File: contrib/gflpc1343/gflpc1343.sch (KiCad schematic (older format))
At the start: 38 parts, among them J1 USB-MICRO-B, P1 GOODFET, P2 SWD, P3 ISP, P4 EXPANSION, Q1 PNP, U1 LPC1343FBD48, U2 AP7333, X1 XTAL4PIN

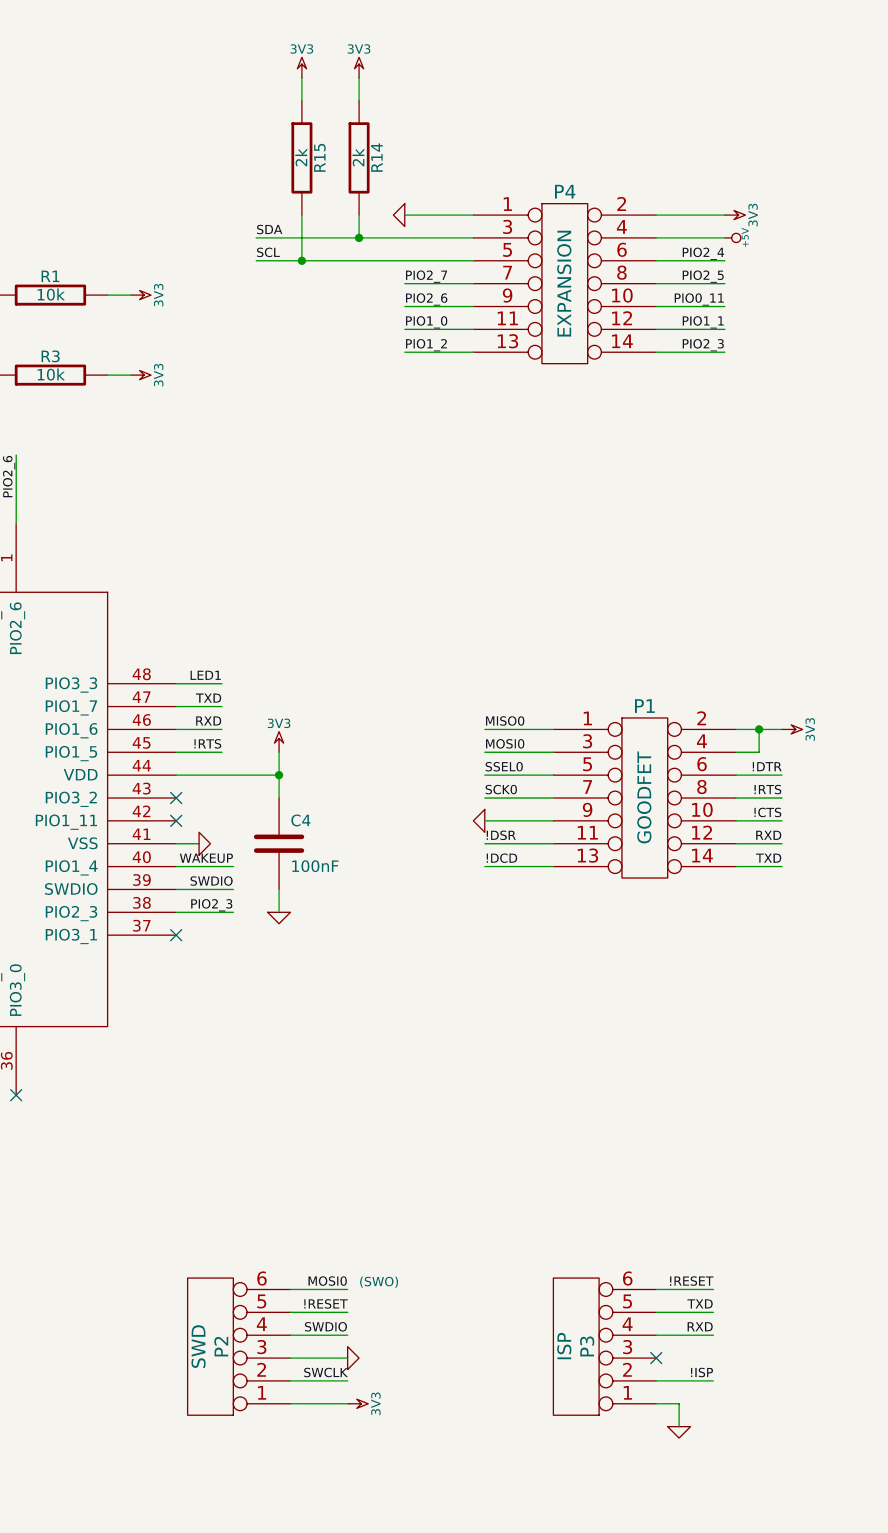
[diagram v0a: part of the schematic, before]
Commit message: gflpc1343 parts selection, paste clearance
git-svn-id: https://svn.code.sf.net/p/goodfet/code@1323 12e2690d-a6be-4b82-a7b7-67c4a43b65c8
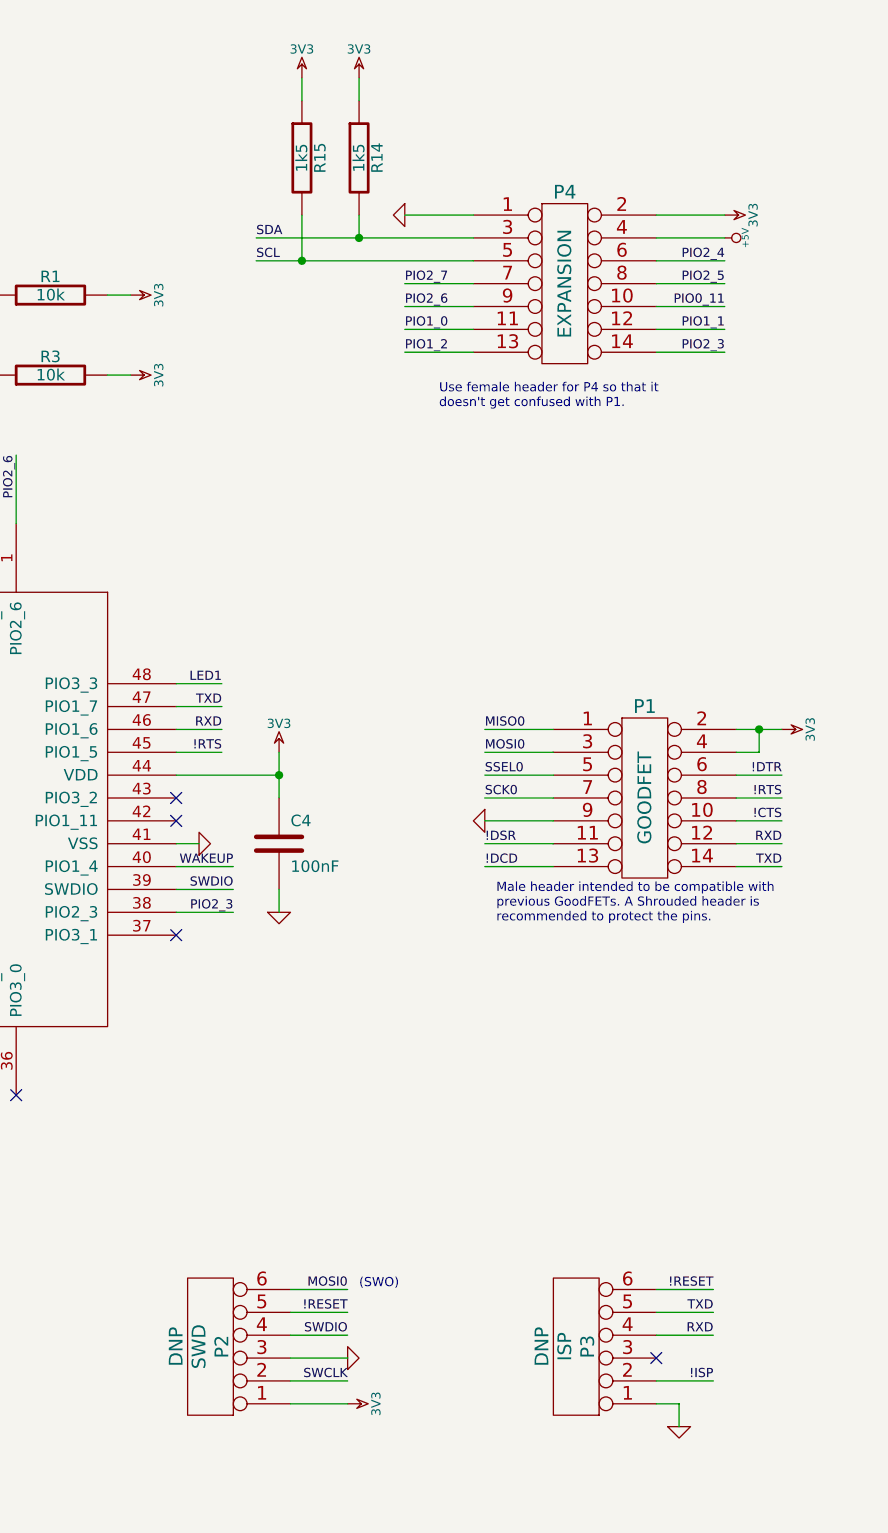
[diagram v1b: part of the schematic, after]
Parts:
- C1, C2, C5, C6: Description (none) -> CAP CER 18PF 50V 5% NP0 0603; Manufacturer (none) -> Murata; Part Number (none) -> GRM1885C1H180JA01D
- C3, C4: Description (none) -> CAP CER 0.1UF 16V 10% X7R 0603; Manufacturer (none) -> Murata; Part Number (none) -> GRM188R71C104KA01D
- C8: Description (none) -> CAP CER 1UF 10V 10% X7R 0603; Manufacturer (none) -> Taiyo Yuden; Part Number (none) -> LMK107B7105KA-T
- P1: Description (none) -> CONN HEADER VERT 14POS GOLD SHROUDED; Manufacturer (none) -> On Shore; Part Number (none) -> 302-S141
- P2, P3: Note (none) -> DNP
- P4: Description (none) -> CONN HEADER FMAL 14PS.1\" DL GOLD; Manufacturer (none) -> Sullins; Part Number (none) -> PPPC072LFBN-RC
- R1, R16, R2, R3, R5: Description (none) -> RES 10K OHM 1/10W 5% 0603 SMD; Manufacturer (none) -> Panasonic; Part Number (none) -> ERJ-3GEYJ103V
- R10, R11, R12, R13: Description (none) -> RES 330 OHM 1/10W 5% 0603 SMD; Manufacturer (none) -> Panasonic; Part Number (none) -> ERJ-3GEYJ331V
- R14, R15: value 2k -> 1k5; Description (none) -> RES 1.5K OHM 1/10W 5% 0603 SMD; Manufacturer (none) -> Panasonic; Part Number (none) -> ERJ-3GEYJ152V
- R4, R6: Description (none) -> RES 1.5K OHM 1/10W 5% 0603 SMD; Manufacturer (none) -> Panasonic; Part Number (none) -> ERJ-3GEYJ152V
- R7: Description (none) -> RES 22K OHM 1/10W 5% 0603 SMD; Manufacturer (none) -> Panasonic; Part Number (none) -> ERJ-3GEYJ223V
- R8, R9: Description (none) -> RES 33.0 OHM 1/10W 1% 0603 SMD; Manufacturer (none) -> Panasonic; Part Number (none) -> ERJ-3EKF33R0V
- U1: Description (none) -> IC MCU 32BIT 32KB FLASH 48LQFP; Manufacturer (none) -> NXP; Part Number (none) -> LPC1343FBD48,151
- U2: Description (none) -> IC REG LDO 3.3V .3A SOT23; Manufacturer (none) -> Diodes Inc.; Part Number (none) -> AP7333-33SAG-7
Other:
- note added: "Male header intended to be compatible with\nprevious GoodFETs. A Shrouded header is\nrecommended to protect the pins."
- note added: "Use female header for P4 so that it\ndoesn't get confused with P1."
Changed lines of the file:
@@
-EESchema Schematic File Version 2  date Tue Sep 18 22:48:30 2012
+EESchema Schematic File Version 2  date Wed Nov  7 13:57:15 2012
 LIBS:power
 LIBS:device
@@
 Sheet 1 1
 Title "gflpc1343"
-Date "18 sep 2012"
+Date "7 nov 2012"
 Rev "$Rev$"
 Comp "Copyright 2012 Michael Ossmann"
@@
 Comment4 ""
 $EndDescr
+Text Notes 9500 4650 0    40   ~ 0
+Male header intended to be compatible with\nprevious GoodFETs. A Shrouded header is\nrecommended to protect the pins.
+Text Notes 9250 2400 0    40   ~ 0
+Use female header for P4 so that it\ndoesn't get confused with P1.
 Wire Wire Line
 	10200 1750 10500 1750
@@
 F 0 "R16" V 4030 6200 50  0000 C CNN
 F 1 "10k" V 3950 6200 50  0000 C CNN
-F 4 "DNP" V 3850 6200 60  0000 C CNN "Note"
+F 4 "Panasonic" H 3950 6200 60  0001 C CNN "Manufacturer"
+F 5 "ERJ-3GEYJ103V" H 3950 6200 60  0001 C CNN "Part Number"
+F 6 "RES 10K OHM 1/10W 5% 0603 SMD" H 3950 6200 60  0001 C CNN "Description"
+F 7 "DNP" V 3850 6200 60  0000 C CNN "Note"
 	1    3950 6200
 	1    0    0    -1
@@
 F 0 "R13" V 2030 6200 50  0000 C CNN
 F 1 "330" V 1950 6200 50  0000 C CNN
+F 4 "Panasonic" H 1950 6200 60  0001 C CNN "Manufacturer"
+F 5 "ERJ-3GEYJ331V" H 1950 6200 60  0001 C CNN "Part Number"
+F 6 "RES 330 OHM 1/10W 5% 0603 SMD" H 1950 6200 60  0001 C CNN "Description"
 	1    1950 6200
 	1    0    0    -1
@@
 P 8650 1300
 F 0 "R15" V 8730 1300 50  0000 C CNN
-F 1 "2k" V 8650 1300 50  0000 C CNN
+F 1 "1k5" V 8650 1300 50  0000 C CNN
+F 4 "Panasonic" H 8650 1300 60  0001 C CNN "Manufacturer"
+F 5 "ERJ-3GEYJ152V" H 8650 1300 60  0001 C CNN "Part Number"
+F 6 "RES 1.5K OHM 1/10W 5% 0603 SMD" H 8650 1300 60  0001 C CNN "Description"
 	1    8650 1300
 	1    0    0    -1
@@
 P 8900 1300
 F 0 "R14" V 8980 1300 50  0000 C CNN
-F 1 "2k" V 8900 1300 50  0000 C CNN
+F 1 "1k5" V 8900 1300 50  0000 C CNN
+F 4 "Panasonic" H 8900 1300 60  0001 C CNN "Manufacturer"
+F 5 "ERJ-3GEYJ152V" H 8900 1300 60  0001 C CNN "Part Number"
+F 6 "RES 1.5K OHM 1/10W 5% 0603 SMD" H 8900 1300 60  0001 C CNN "Description"
 	1    8900 1300
 	1    0    0    -1
@@
 F 0 "P4" H 9800 2250 60  0000 C CNN
 F 1 "EXPANSION" V 9800 1850 60  0000 C CNN
+F 4 "Sullins" H 9800 1850 60  0001 C CNN "Manufacturer"
+F 5 "PPPC072LFBN-RC" H 9800 1850 60  0001 C CNN "Part Number"
+F 6 "CONN HEADER FMAL 14PS.1\" DL GOLD" H 9800 1850 60  0001 C CNN "Description"
 	1    9800 1850
 	1    0    0    -1
@@
 F 0 "P2" V 8200 6500 60  0000 C CNN
 F 1 "SWD" V 8300 6500 60  0000 C CNN
+F 4 "DNP" V 8400 6500 60  0000 C CNN "Note"
 	1    8250 6500
 	-1   0    0    1
@@
 F 0 "P3" V 9800 6500 60  0000 C CNN
 F 1 "ISP" V 9900 6500 60  0000 C CNN
+F 4 "DNP" V 10000 6500 60  0000 C CNN "Note"
 	1    9850 6500
 	-1   0    0    1
@@
 F 0 "R12" V 1730 6200 50  0000 C CNN
 F 1 "330" V 1650 6200 50  0000 C CNN
+F 4 "Panasonic" H 1650 6200 60  0001 C CNN "Manufacturer"
+F 5 "ERJ-3GEYJ331V" H 1650 6200 60  0001 C CNN "Part Number"
+F 6 "RES 330 OHM 1/10W 5% 0603 SMD" H 1650 6200 60  0001 C CNN "Description"
 	1    1650 6200
 	1    0    0    -1
@@
 F 0 "R11" V 1430 6200 50  0000 C CNN
 F 1 "330" V 1350 6200 50  0000 C CNN
+F 4 "Panasonic" H 1350 6200 60  0001 C CNN "Manufacturer"
+F 5 "ERJ-3GEYJ331V" H 1350 6200 60  0001 C CNN "Part Number"
+F 6 "RES 330 OHM 1/10W 5% 0603 SMD" H 1350 6200 60  0001 C CNN "Description"
 	1    1350 6200
 	1    0    0    -1
@@
 F 0 "R10" V 1130 6200 50  0000 C CNN
 F 1 "330" V 1050 6200 50  0000 C CNN
+F 4 "Panasonic" H 1050 6200 60  0001 C CNN "Manufacturer"
+F 5 "ERJ-3GEYJ331V" H 1050 6200 60  0001 C CNN "Part Number"
+F 6 "RES 330 OHM 1/10W 5% 0603 SMD" H 1050 6200 60  0001 C CNN "Description"
 	1    1050 6200
 	1    0    0    -1
@@
 F 0 "R7" V 4380 3400 50  0000 C CNN
 F 1 "22k" V 4300 3400 50  0000 C CNN
+F 4 "Panasonic" H 4300 3400 60  0001 C CNN "Manufacturer"
+F 5 "ERJ-3GEYJ223V" H 4300 3400 60  0001 C CNN "Part Number"
+F 6 "RES 22K OHM 1/10W 5% 0603 SMD" H 4300 3400 60  0001 C CNN "Description"
 	1    4300 3400
 	1    0    0    -1
@@
 F 0 "R5" V 4380 2700 50  0000 C CNN
 F 1 "10k" V 4300 2700 50  0000 C CNN
+F 4 "Panasonic" H 4300 2700 60  0001 C CNN "Manufacturer"
+F 5 "ERJ-3GEYJ103V" H 4300 2700 60  0001 C CNN "Part Number"
+F 6 "RES 10K OHM 1/10W 5% 0603 SMD" H 4300 2700 60  0001 C CNN "Description"
 	1    4300 2700
 	1    0    0    -1
@@
 F 0 "C8" H 1700 1550 50  0000 L CNN
 F 1 "1uF" H 1700 1350 50  0000 L CNN
+F 4 "Taiyo Yuden" H 1650 1450 60  0001 C CNN "Manufacturer"
+F 5 "LMK107B7105KA-T" H 1650 1450 60  0001 C CNN "Part Number"
+F 6 "CAP CER 1UF 10V 10% X7R 0603" H 1650 1450 60  0001 C CNN "Description"
 	1    1650 1450
 	1    0    0    -1
@@
 F 0 "U2" H 2250 1300 60  0000 C CNN
 F 1 "AP7333" H 2250 900 60  0000 C CNN
+F 4 "Diodes Inc." H 2250 1100 60  0001 C CNN "Manufacturer"
+F 5 "AP7333-33SAG-7" H 2250 1100 60  0001 C CNN "Part Number"
+F 6 "IC REG LDO 3.3V .3A SOT23" H 2250 1100 60  0001 C CNN "Description"
 	1    2250 1100
 	1    0    0    -1
@@
 F 0 "R3" V 7630 2250 50  0000 C CNN
 F 1 "10k" V 7550 2250 50  0000 C CNN
+F 4 "Panasonic" H 7550 2250 60  0001 C CNN "Manufacturer"
+F 5 "ERJ-3GEYJ103V" H 7550 2250 60  0001 C CNN "Part Number"
+F 6 "RES 10K OHM 1/10W 5% 0603 SMD" H 7550 2250 60  0001 C CNN "Description"
 	1    7550 2250
 	0    -1   -1   0
@@
 F 0 "C3" H 6450 2450 50  0000 L CNN
 F 1 "100nF" H 6450 2250 50  0000 L CNN
+F 4 "Murata" H 6400 2350 60  0001 C CNN "Manufacturer"
+F 5 "GRM188R71C104KA01D" H 6400 2350 60  0001 C CNN "Part Number"
+F 6 "CAP CER 0.1UF 16V 10% X7R 0603" H 6400 2350 60  0001 C CNN "Description"
 	1    6400 2350
 	0    -1   -1   0
@@
 F 0 "C4" H 8600 4400 50  0000 L CNN
 F 1 "100nF" H 8600 4200 50  0000 L CNN
+F 4 "Murata" H 8550 4300 60  0001 C CNN "Manufacturer"
+F 5 "GRM188R71C104KA01D" H 8550 4300 60  0001 C CNN "Part Number"
+F 6 "CAP CER 0.1UF 16V 10% X7R 0603" H 8550 4300 60  0001 C CNN "Description"
 	1    8550 4300
 	1    0    0    -1
@@
 F 0 "R2" V 2930 2250 50  0000 C CNN
 F 1 "10k" V 2850 2250 50  0000 C CNN
+F 4 "Panasonic" H 2850 2250 60  0001 C CNN "Manufacturer"
+F 5 "ERJ-3GEYJ103V" H 2850 2250 60  0001 C CNN "Part Number"
+F 6 "RES 10K OHM 1/10W 5% 0603 SMD" H 2850 2250 60  0001 C CNN "Description"
 	1    2850 2250
 	1    0    0    -1
@@
 F 0 "R4" V 3280 2600 50  0000 C CNN
 F 1 "1k5" V 3200 2600 50  0000 C CNN
+F 4 "Panasonic" H 3200 2600 60  0001 C CNN "Manufacturer"
+F 5 "ERJ-3GEYJ152V" H 3200 2600 60  0001 C CNN "Part Number"
+F 6 "RES 1.5K OHM 1/10W 5% 0603 SMD" H 3200 2600 60  0001 C CNN "Description"
 	1    3200 2600
 	0    -1   -1   0
@@
 F 0 "R1" V 7630 1900 50  0000 C CNN
 F 1 "10k" V 7550 1900 50  0000 C CNN
+F 4 "Panasonic" H 7550 1900 60  0001 C CNN "Manufacturer"
+F 5 "ERJ-3GEYJ103V" H 7550 1900 60  0001 C CNN "Part Number"
+F 6 "RES 10K OHM 1/10W 5% 0603 SMD" H 7550 1900 60  0001 C CNN "Description"
 	1    7550 1900
 	0    -1   -1   0
@@
 F 0 "C5" H 2200 4700 50  0000 L CNN
 F 1 "18pF" H 2200 4500 50  0000 L CNN
+F 4 "Murata" H 2150 4600 60  0001 C CNN "Manufacturer"
+F 5 "GRM1885C1H180JA01D" H 2150 4600 60  0001 C CNN "Part Number"
+F 6 "CAP CER 18PF 50V 5% NP0 0603" H 2150 4600 60  0001 C CNN "Description"
 	1    2150 4600
 	1    0    0    -1
@@
 F 0 "C6" H 2500 4700 50  0000 L CNN
 F 1 "18pF" H 2500 4500 50  0000 L CNN
+F 4 "Murata" H 2450 4600 60  0001 C CNN "Manufacturer"
+F 5 "GRM1885C1H180JA01D" H 2450 4600 60  0001 C CNN "Part Number"
+F 6 "CAP CER 18PF 50V 5% NP0 0603" H 2450 4600 60  0001 C CNN "Description"
 	1    2450 4600
 	1    0    0    -1
@@
 F 0 "R6" V 2530 3150 50  0000 C CNN
 F 1 "1k5" V 2450 3150 50  0000 C CNN
+F 4 "Panasonic" H 2450 3150 60  0001 C CNN "Manufacturer"
+F 5 "ERJ-3GEYJ152V" H 2450 3150 60  0001 C CNN "Part Number"
+F 6 "RES 1.5K OHM 1/10W 5% 0603 SMD" H 2450 3150 60  0001 C CNN "Description"
 	1    2450 3150
 	1    0    0    -1
@@
 F 0 "R8" V 2230 3850 50  0000 C CNN
 F 1 "33" V 2150 3850 50  0000 C CNN
+F 4 "Panasonic" H 2150 3850 60  0001 C CNN "Manufacturer"
+F 5 "ERJ-3EKF33R0V" H 2150 3850 60  0001 C CNN "Part Number"
+F 6 "RES 33.0 OHM 1/10W 1% 0603 SMD" H 2150 3850 60  0001 C CNN "Description"
 	1    2150 3850
 	-1   0    0    1
@@
 F 0 "R9" V 2530 3850 50  0000 C CNN
 F 1 "33" V 2450 3850 50  0000 C CNN
+F 4 "Panasonic" H 2450 3850 60  0001 C CNN "Manufacturer"
+F 5 "ERJ-3EKF33R0V" H 2450 3850 60  0001 C CNN "Part Number"
+F 6 "RES 33.0 OHM 1/10W 1% 0603 SMD" H 2450 3850 60  0001 C CNN "Description"
 	1    2450 3850
 	-1   0    0    1
@@
 F 0 "C1" H 5350 1300 50  0000 L CNN
 F 1 "18pF" H 5350 1100 50  0000 L CNN
+F 4 "Murata" H 5300 1200 60  0001 C CNN "Manufacturer"
+F 5 "GRM1885C1H180JA01D" H 5300 1200 60  0001 C CNN "Part Number"
+F 6 "CAP CER 18PF 50V 5% NP0 0603" H 5300 1200 60  0001 C CNN "Description"
 	1    5300 1200
 	1    0    0    -1
@@
 F 0 "C2" H 6150 1300 50  0000 L CNN
 F 1 "18pF" H 6150 1100 50  0000 L CNN
+F 4 "Murata" H 6100 1200 60  0001 C CNN "Manufacturer"
+F 5 "GRM1885C1H180JA01D" H 6100 1200 60  0001 C CNN "Part Number"
+F 6 "CAP CER 18PF 50V 5% NP0 0603" H 6100 1200 60  0001 C CNN "Description"
 	1    6100 1200
 	1    0    0    -1
@@
 F 0 "U1" H 6850 4250 60  0000 C CNN
 F 1 "LPC1343FBD48" H 6850 4050 60  0000 C CNN
+F 4 "NXP" H 6850 4150 60  0001 C CNN "Manufacturer"
+F 5 "LPC1343FBD48,151" H 6850 4150 60  0001 C CNN "Part Number"
+F 6 "IC MCU 32BIT 32KB FLASH 48LQFP" H 6850 4150 60  0001 C CNN "Description"
 	1    6850 4150
 	0    1    1    0
@@
 F 0 "P1" H 10150 4500 60  0000 C CNN
 F 1 "GOODFET" V 10150 4100 60  0000 C CNN
+F 4 "On Shore" H 10150 4100 60  0001 C CNN "Manufacturer"
+F 5 "302-S141" H 10150 4100 60  0001 C CNN "Part Number"
+F 6 "CONN HEADER VERT 14POS GOLD SHROUDED" H 10150 4100 60  0001 C CNN "Description"
 	1    10150 4100
 	1    0    0    -1

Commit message: completed TOAD design
git-svn-id: https://svn.code.sf.net/p/goodfet/code@1656 12e2690d-a6be-4b82-a7b7-67c4a43b65c8
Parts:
- D1, D4: Description (none) -> LED GREEN STD BRIGHT 0603 SMD; Manufacturer (none) -> Everlight; Part Number (none) -> QTLP601C4TR
- D2: Description (none) -> LED RED STD BRIGHT 0603 SMD; Manufacturer (none) -> Everlight; Part Number (none) -> QTLP601CRTR
- D3: Description (none) -> LED YLW SUPER BRIGHT 0606 SMD; Manufacturer (none) -> Everlight; Part Number (none) -> QTLP600CYTR
- P4: Description CONN HEADER FMAL 14PS.1\" DL GOLD -> CONN HEADR FMALE 14POS .1\" DL AU; Part Number PPPC072LFBN-RC -> SFH11-PBPC-D07-ST-BK
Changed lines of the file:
@@
-EESchema Schematic File Version 2  date Wed Nov  7 13:57:15 2012
+EESchema Schematic File Version 2  date Thu Aug 22 00:59:04 2013
 LIBS:power
 LIBS:device
@@
 LIBS:gflpc
 LIBS:gflpc1343-cache
-EELAYER 25  0
+EELAYER 27 0
 EELAYER END
-$Descr A4 11700 8267
+$Descr A4 11693 8268
 encoding utf-8
 Sheet 1 1
 Title "gflpc1343"
-Date "7 nov 2012"
+Date "22 aug 2013"
 Rev "$Rev$"
 Comp "Copyright 2012 Michael Ossmann"
@@
 F 0 "D4" H 1950 6850 50  0000 C CNN
 F 1 "LED2" H 1950 6650 50  0000 C CNN
+F 4 "Everlight" H 1950 6750 60  0001 C CNN "Manufacturer"
+F 5 "QTLP601C4TR" H 1950 6750 60  0001 C CNN "Part Number"
+F 6 "LED GREEN STD BRIGHT 0603 SMD" H 1950 6750 60  0001 C CNN "Description"
 	1    1950 6750
 	0    1    1    0
@@
 F 1 "EXPANSION" V 9800 1850 60  0000 C CNN
 F 4 "Sullins" H 9800 1850 60  0001 C CNN "Manufacturer"
-F 5 "PPPC072LFBN-RC" H 9800 1850 60  0001 C CNN "Part Number"
-F 6 "CONN HEADER FMAL 14PS.1\" DL GOLD" H 9800 1850 60  0001 C CNN "Description"
+F 5 "SFH11-PBPC-D07-ST-BK" H 9800 1850 60  0001 C CNN "Part Number"
+F 6 "CONN HEADR FMALE 14POS .1\" DL AU" H 9800 1850 60  0001 C CNN "Description"
 	1    9800 1850
 	1    0    0    -1
@@
 F 0 "D3" H 1650 6850 50  0000 C CNN
 F 1 "LED1" H 1650 6650 50  0000 C CNN
+F 4 "Everlight" H 1650 6750 60  0001 C CNN "Manufacturer"
+F 5 "QTLP600CYTR" H 1650 6750 60  0001 C CNN "Part Number"
+F 6 "LED YLW SUPER BRIGHT 0606 SMD" H 1650 6750 60  0001 C CNN "Description"
 	1    1650 6750
 	0    1    1    0
@@
 F 0 "D2" H 1350 6850 50  0000 C CNN
 F 1 "TXLED" H 1350 6650 50  0000 C CNN
+F 4 "Everlight" H 1350 6750 60  0001 C CNN "Manufacturer"
+F 5 "QTLP601CRTR" H 1350 6750 60  0001 C CNN "Part Number"
+F 6 "LED RED STD BRIGHT 0603 SMD" H 1350 6750 60  0001 C CNN "Description"
 	1    1350 6750
 	0    1    1    0
@@
 F 0 "D1" H 1050 6850 50  0000 C CNN
 F 1 "RXLED" H 1050 6650 50  0000 C CNN
+F 4 "Everlight" H 1050 6750 60  0001 C CNN "Manufacturer"
+F 5 "QTLP601C4TR" H 1050 6750 60  0001 C CNN "Part Number"
+F 6 "LED GREEN STD BRIGHT 0603 SMD" H 1050 6750 60  0001 C CNN "Description"
 	1    1050 6750
 	0    1    1    0
